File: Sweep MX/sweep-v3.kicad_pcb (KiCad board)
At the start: 2 copper layers, 229.5 x 95.2 mm, 42 parts, among them J1 AudioJack4dpb, J2 AudioJack4dpb, SW10 SW_Push, SW11 SW_Push, SW11_r1 SW_Push, SW12 SW_Push, SW12_r1 SW_Push, SW13_r1 SW_Push, SW14 SW_Push, SW15 SW_Push, SW15_r1 SW_Push, SW16 SW_Push, SW16_r1 SW_Push, SW17 SW_Push, SW17_r1 SW_Push, SW18 SW_Push, SW18_r1 SW_Push, SW2 SW_Push, SW20 SW_Push, SW20_r1 SW_Push, SW21 SW_Push, SW21_r1 SW_Push, SW2_r1 SW_Push, SW3 SW_Push, SW3_r1 SW_Push, SW4 SW_Push, SW4_r1 SW_Push, SW5 SW_Push, SW5_r1 SW_Push, SW6 SW_Push, SW6_r1 SW_Push, SW7_r1 SW_Push, SW8 SW_Push, SW8_r1 SW_Push, SW9 SW_Push, SW9_r1 SW_Push, U1 ProMicro-kbd, U2 ProMicro-kbd

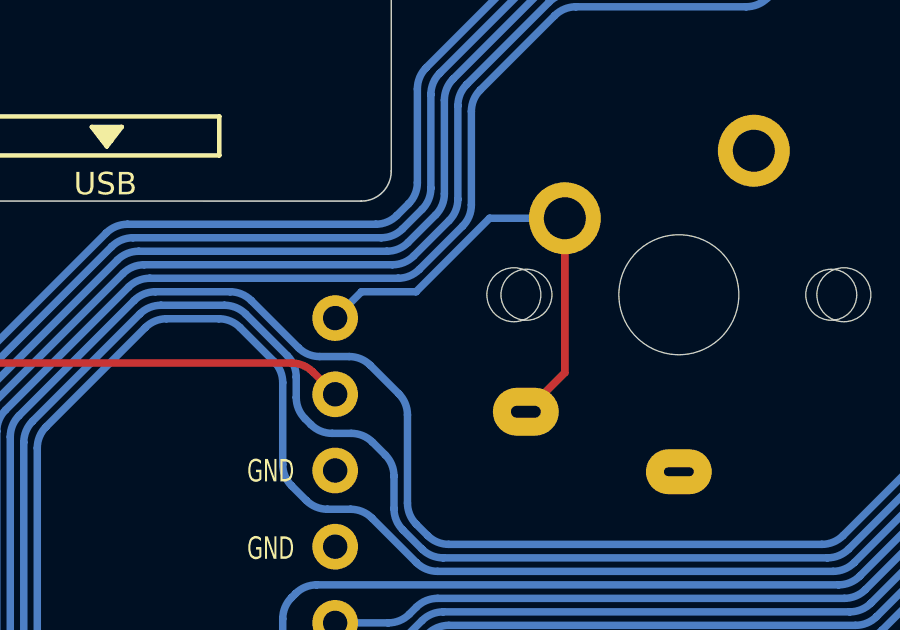
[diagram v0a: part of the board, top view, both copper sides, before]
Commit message: Add v4 with halftone silks
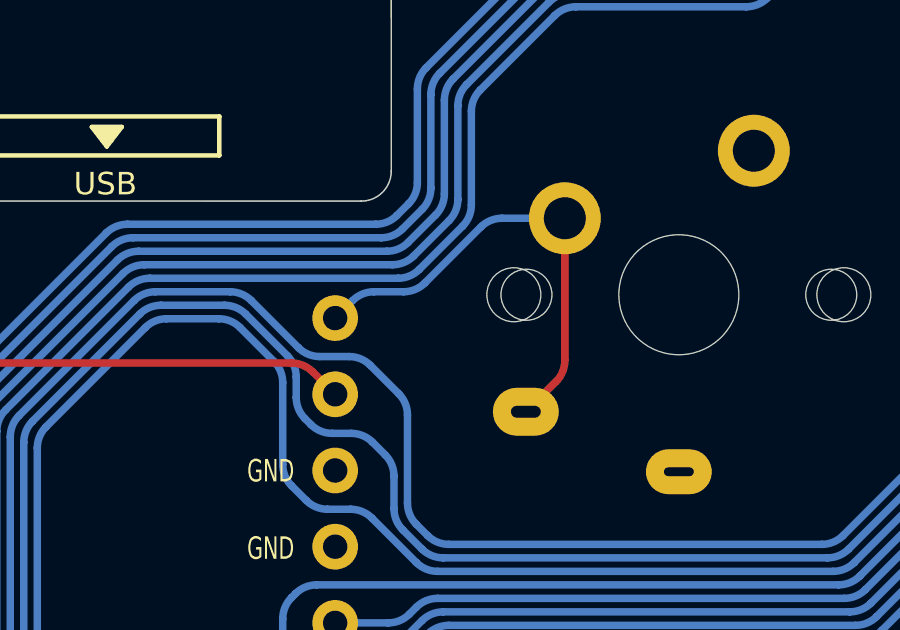
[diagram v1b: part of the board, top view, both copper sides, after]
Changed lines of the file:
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@@
   (arc (start 169.352893 92.432893) (mid 169.028469 92.21612) (end 168.645786 92.14) (width 0.25) (layer "B.Cu") (net 25))
   (arc (start 166.381802 87.918808) (mid 166.305682 87.536124) (end 166.088909 87.211701) (width 0.25) (layer "B.Cu") (net 25))
-  (segment (start 175.78584 87.59) (end 174.48584 88.89) (width 0.25) (layer "F.Cu") (net 26))
-  (segment (start 175.78584 82.44) (end 175.78584 87.59) (width 0.25) (layer "F.Cu") (net 26))
-  (segment (start 173.276396 82.44) (end 175.78584 82.44) (width 0.25) (layer "B.Cu") (net 26))
-  (segment (start 168.12924 85.768) (end 169.00724 84.89) (width 0.25) (layer "B.Cu") (net 26))
-  (segment (start 170.826396 84.89) (end 173.276396 82.44) (width 0.25) (layer "B.Cu") (net 26))
-  (segment (start 169.00724 84.89) (end 170.826396 84.89) (width 0.25) (layer "B.Cu") (net 26))
+  (segment (start 175.492947 87.882893) (end 174.48584 88.89) (width 0.25) (layer "F.Cu") (net 26))
+  (segment (start 175.78584 82.44) (end 175.78584 87.175786) (width 0.25) (layer "F.Cu") (net 26))
+  (arc (start 175.492947 87.882893) (mid 175.70972 87.55847) (end 175.78584 87.175786) (width 0.25) (layer "F.Cu") (net 26))
+  (segment (start 173.69061 82.44) (end 175.78584 82.44) (width 0.25) (layer "B.Cu") (net 26))
+  (segment (start 168.12924 85.768) (end 168.714347 85.182893) (width 0.25) (layer "B.Cu") (net 26))
+  (segment (start 171.119289 84.597107) (end 172.983503 82.732893) (width 0.25) (layer "B.Cu") (net 26))
+  (segment (start 169.421454 84.89) (end 170.412182 84.89) (width 0.25) (layer "B.Cu") (net 26))
+  (arc (start 171.119289 84.597107) (mid 170.794866 84.81388) (end 170.412182 84.89) (width 0.25) (layer "B.Cu") (net 26))
+  (arc (start 173.69061 82.44) (mid 173.307927 82.51612) (end 172.983503 82.732893) (width 0.25) (layer "B.Cu") (net 26))
+  (arc (start 168.714347 85.182893) (mid 169.03877 84.96612) (end 169.421454 84.89) (width 0.25) (layer "B.Cu") (net 26))
   (segment (start 251.538947 117.892893) (end 250.53184 118.9) (width 0.25) (layer "F.Cu") (net 27))
   (segment (start 251.83184 112.45) (end 251.83184 117.185786) (width 0.25) (layer "F.Cu") (net 27))
